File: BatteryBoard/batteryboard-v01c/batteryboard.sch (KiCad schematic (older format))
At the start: 27 parts, among them J1 KEYSTONE-1042, J12 Screw_Terminal_01x02, J2 KEYSTONE-1042, J3 KEYSTONE-1042, J4 KEYSTONE-1042, J5 KEYSTONE-1042, J6 KEYSTONE-1042, J7 5023520400, J8 Screw_Terminal_01x02, Q1 IRF7458, Q2 IRF7458, U1 R5460N233AF

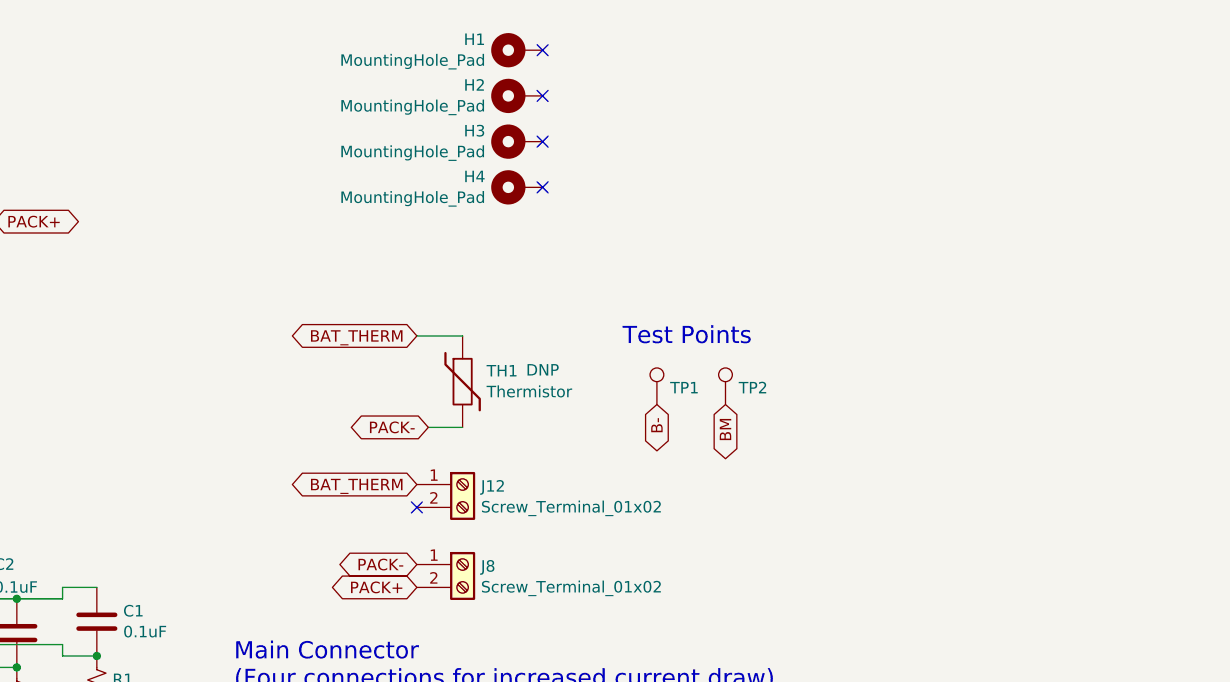
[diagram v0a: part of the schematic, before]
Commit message: Added simple thermistor circuit with logic switch to activate.
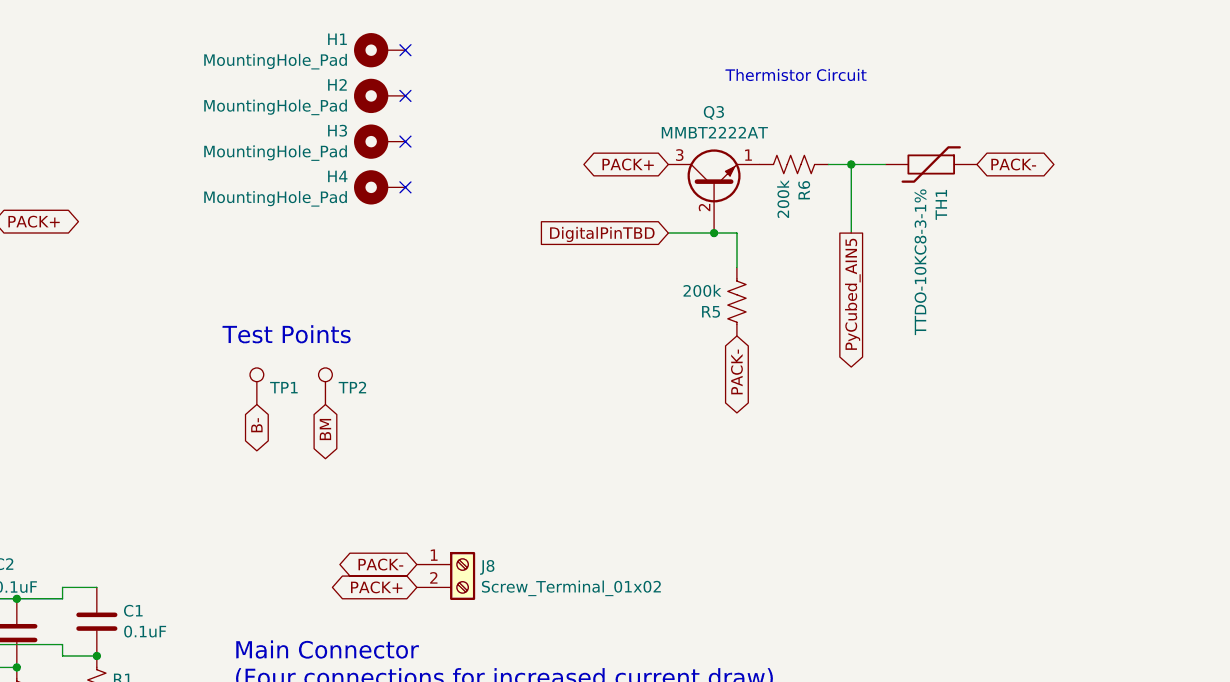
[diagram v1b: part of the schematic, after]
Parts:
- removed J12: Screw_Terminal_01x02, batteryboard:pheonix_2pos_screwterminal, symbol Connector:Screw_Terminal_01x02
- added Q3: MMBT2222AT, Package_TO_SOT_THT:TO-39-3, symbol Transistor_BJT:2N2219
- added R5, R6: 200k, Resistor_SMD:R_0603_1608Metric, symbol Device:R_US
- TH1: value Thermistor -> TTDO-10KC8-3-1%; DNP DNP -> (none)
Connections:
- net BAT_THERM is gone; now on net PACK-: TH1.1
- net PACK+: now also Q3.3 (C)
- net PACK-: now also R5.2; no longer TH1.2
- new net: Q3.1 (E), R6.1
- new net DigitalPinTBD: Q3.2 (B), R5.1
- new net PyCubed_AIN5: R6.2, TH1.2
- no-connect marks 5 -> 4
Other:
- note added: "Thermistor Circuit"
- moved on the sheet: H1, H2, H3, H4, TP1, TP2
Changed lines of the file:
@@
 L Connector:TestPoint TP1
 U 1 1 5E18DFC3
-P 6650 2550
-F 0 "TP1" H 6708 2622 50  0000 L CNN
-F 1 "TestPoint" H 6708 2577 50  0001 L CNN
-F 2 "TestPoint:TestPoint_Loop_D1.80mm_Drill1.0mm_Beaded" H 6850 2550 50  0001 C CNN
-F 3 "~" H 6850 2550 50  0001 C CNN
-F 4 "DNP" H 6650 2550 50  0001 C CNN "DNP"
-	1    6650 2550
+P 4900 2550
+F 0 "TP1" H 4958 2622 50  0000 L CNN
+F 1 "TestPoint" H 4958 2577 50  0001 L CNN
+F 2 "TestPoint:TestPoint_Loop_D1.80mm_Drill1.0mm_Beaded" H 5100 2550 50  0001 C CNN
+F 3 "~" H 5100 2550 50  0001 C CNN
+F 4 "DNP" H 4900 2550 50  0001 C CNN "DNP"
+	1    4900 2550
 	1    0    0    -1
 $EndComp
@@
 L Connector:TestPoint TP2
 U 1 1 5E18E53B
-P 6950 2550
-F 0 "TP2" H 7008 2622 50  0000 L CNN
-F 1 "TestPoint" H 7008 2577 50  0001 L CNN
-F 2 "TestPoint:TestPoint_Loop_D1.80mm_Drill1.0mm_Beaded" H 7150 2550 50  0001 C CNN
-F 3 "~" H 7150 2550 50  0001 C CNN
-F 4 "DNP" H 6950 2550 50  0001 C CNN "DNP"
-	1    6950 2550
-	1    0    0    -1
-$EndComp
-Text GLabel 6650 2550 3    50   BiDi ~ 0
+P 5200 2550
+F 0 "TP2" H 5258 2622 50  0000 L CNN
+F 1 "TestPoint" H 5258 2577 50  0001 L CNN
+F 2 "TestPoint:TestPoint_Loop_D1.80mm_Drill1.0mm_Beaded" H 5400 2550 50  0001 C CNN
+F 3 "~" H 5400 2550 50  0001 C CNN
+F 4 "DNP" H 5200 2550 50  0001 C CNN "DNP"
+	1    5200 2550
+	1    0    0    -1
+$EndComp
+Text GLabel 4900 2550 3    50   BiDi ~ 0
 B-
-Text GLabel 6950 2550 3    50   BiDi ~ 0
+Text GLabel 5200 2550 3    50   BiDi ~ 0
 BM
 Text GLabel 5600 3250 0    50   BiDi ~ 0
@@
 Text GLabel 5600 3350 0    50   BiDi ~ 0
 PACK+
-$Comp
-L Device:Thermistor TH1
-U 1 1 5E1E69F6
-P 5800 2450
-F 0 "TH1" H 5905 2496 50  0000 L CNN
-F 1 "Thermistor" H 5905 2405 50  0000 L CNN
-F 2 "Resistor_THT:R_Axial_DIN0204_L3.6mm_D1.6mm_P5.08mm_Horizontal" H 5800 2450 50  0001 C CNN
-F 3 "~" H 5800 2450 50  0001 C CNN
-F 4 "DNP" H 6150 2500 50  0000 C CNN "DNP"
-	1    5800 2450
-	1    0    0    -1
-$EndComp
-Text GLabel 5650 2650 0    50   BiDi ~ 0
-PACK-
-Wire Wire Line
-	5650 2650 5800 2650
-Text GLabel 5600 2250 0    50   BiDi ~ 0
-BAT_THERM
-Wire Wire Line
-	5600 2250 5800 2250
-Text GLabel 5600 2900 0    50   BiDi ~ 0
-BAT_THERM
 Text Notes 1650 950  0    50   ~ 0
 Must install low-side before high-side
@@
 Text Notes 1650 2550 0    50   ~ 0
 One from this \ngroup first
-Text Notes 6500 2300 0    75   ~ 0
+Text Notes 4750 2300 0    75   ~ 0
 Test Points
 Text Notes 2350 3050 0    75   ~ 0
@@
 L Mechanical:MountingHole_Pad H1
 U 1 1 5E6C3943
-P 6050 1000
-F 0 "H1" V 6004 1150 50  0000 L CNN
-F 1 "MountingHole_Pad" V 6095 1150 50  0000 L CNN
-F 2 "custom-footprints:MountingHole_3.2mm_M3_DIN965_PadMOD" H 6050 1000 50  0001 C CNN
-F 3 "~" H 6050 1000 50  0001 C CNN
-F 4 "DNP" H 6050 1000 50  0001 C CNN "DNP"
-	1    6050 1000
+P 5450 1000
+F 0 "H1" V 5404 1150 50  0000 L CNN
+F 1 "MountingHole_Pad" V 5495 1150 50  0000 L CNN
+F 2 "custom-footprints:MountingHole_3.2mm_M3_DIN965_PadMOD" H 5450 1000 50  0001 C CNN
+F 3 "~" H 5450 1000 50  0001 C CNN
+F 4 "DNP" H 5450 1000 50  0001 C CNN "DNP"
+	1    5450 1000
 	0    -1   1    0
 $EndComp
@@
 L Mechanical:MountingHole_Pad H2
 U 1 1 5E6C65C6
-P 6050 1200
-F 0 "H2" V 6004 1350 50  0000 L CNN
-F 1 "MountingHole_Pad" V 6095 1350 50  0000 L CNN
-F 2 "custom-footprints:MountingHole_3.2mm_M3_DIN965_PadMOD" H 6050 1200 50  0001 C CNN
-F 3 "~" H 6050 1200 50  0001 C CNN
-F 4 "DNP" H 6050 1200 50  0001 C CNN "DNP"
-	1    6050 1200
+P 5450 1200
+F 0 "H2" V 5404 1350 50  0000 L CNN
+F 1 "MountingHole_Pad" V 5495 1350 50  0000 L CNN
+F 2 "custom-footprints:MountingHole_3.2mm_M3_DIN965_PadMOD" H 5450 1200 50  0001 C CNN
+F 3 "~" H 5450 1200 50  0001 C CNN
+F 4 "DNP" H 5450 1200 50  0001 C CNN "DNP"
+	1    5450 1200
 	0    -1   1    0
 $EndComp
@@
 L Mechanical:MountingHole_Pad H3
 U 1 1 5E6C7B02
-P 6050 1400
-F 0 "H3" V 6004 1550 50  0000 L CNN
-F 1 "MountingHole_Pad" V 6095 1550 50  0000 L CNN
-F 2 "custom-footprints:MountingHole_3.2mm_M3_DIN965_PadMOD" H 6050 1400 50  0001 C CNN
-F 3 "~" H 6050 1400 50  0001 C CNN
-F 4 "DNP" H 6050 1400 50  0001 C CNN "DNP"
-	1    6050 1400
+P 5450 1400
+F 0 "H3" V 5404 1550 50  0000 L CNN
+F 1 "MountingHole_Pad" V 5495 1550 50  0000 L CNN
+F 2 "custom-footprints:MountingHole_3.2mm_M3_DIN965_PadMOD" H 5450 1400 50  0001 C CNN
+F 3 "~" H 5450 1400 50  0001 C CNN
+F 4 "DNP" H 5450 1400 50  0001 C CNN "DNP"
+	1    5450 1400
 	0    -1   1    0
 $EndComp
@@
 L Mechanical:MountingHole_Pad H4
 U 1 1 5E6C7E13
-P 6050 1600
-F 0 "H4" V 6004 1750 50  0000 L CNN
-F 1 "MountingHole_Pad" V 6095 1750 50  0000 L CNN
-F 2 "custom-footprints:MountingHole_3.2mm_M3_DIN965_PadMOD" H 6050 1600 50  0001 C CNN
-F 3 "~" H 6050 1600 50  0001 C CNN
-F 4 "DNP" H 6050 1600 50  0001 C CNN "DNP"
-	1    6050 1600
-	0    -1   1    0
-$EndComp
-NoConn ~ 6150 1000
-NoConn ~ 6150 1200
-NoConn ~ 6150 1400
-NoConn ~ 6150 1600
+P 5450 1600
+F 0 "H4" V 5404 1750 50  0000 L CNN
+F 1 "MountingHole_Pad" V 5495 1750 50  0000 L CNN
+F 2 "custom-footprints:MountingHole_3.2mm_M3_DIN965_PadMOD" H 5450 1600 50  0001 C CNN
+F 3 "~" H 5450 1600 50  0001 C CNN
+F 4 "DNP" H 5450 1600 50  0001 C CNN "DNP"
+	1    5450 1600
+	0    -1   1    0
+$EndComp
+NoConn ~ 5550 1000
+NoConn ~ 5550 1200
+NoConn ~ 5550 1400
+NoConn ~ 5550 1600
 Text GLabel 6900 4300 2    50   BiDi ~ 0
 PACK-
@@
 Text GLabel 5300 4300 0    50   BiDi ~ 0
 PACK+
-NoConn ~ 5600 3000
-$Comp
-L Connector:Screw_Terminal_01x02 J12
-U 1 1 5E1A7D63
-P 5800 2900
-F 0 "J12" H 5880 2892 50  0000 L CNN
-F 1 "Screw_Terminal_01x02" H 5880 2801 50  0000 L CNN
-F 2 "batteryboard:pheonix_2pos_screwterminal" H 5800 2900 50  0001 C CNN
-F 3 "~" H 5800 2900 50  0001 C CNN
-F 4 "DNP" H 5800 2900 50  0001 C CNN "DNP"
-	1    5800 2900
-	1    0    0    -1
-$EndComp
 $Comp
 L Connector:Screw_Terminal_01x02 J8
@@
 	1    0    0    -1
 $EndComp
+Text Notes 6950 1150 0    50   ~ 0
+Thermistor Circuit
+Text GLabel 6700 1500 0    50   BiDi ~ 0
+PACK+
+$Comp
+L Transistor_BJT:2N2219 Q3
+U 1 1 6221ACAF
+P 6900 1600
+F 0 "Q3" V 7228 1600 50  0000 C CNN
+F 1 "MMBT2222AT" V 7137 1600 50  0000 C CNN
+F 2 "Package_TO_SOT_THT:TO-39-3" H 7100 1525 50  0001 L CIN
+F 3 "http://www.onsemi.com/pub_link/Collateral/2N2219-D.PDF" H 6900 1600 50  0001 L CNN
+	1    6900 1600
+	0    -1   -1   0
+$EndComp
+$Comp
+L Device:R_US R6
+U 1 1 6221CAB9
+P 7250 1500
+F 0 "R6" H 7182 1454 50  0000 R CNN
+F 1 "200k" H 7182 1545 50  0000 R CNN
+F 2 "Resistor_SMD:R_0603_1608Metric" V 7290 1490 50  0001 C CNN
+F 3 "~" H 7250 1500 50  0001 C CNN
+	1    7250 1500
+	0    -1   -1   0
+$EndComp
+Wire Wire Line
+	7400 1500 7500 1500
+Wire Wire Line
+	7500 1500 7500 1800
+Wire Wire Line
+	7500 1500 7650 1500
+Connection ~ 7500 1500
+Text GLabel 8050 1500 2    50   BiDi ~ 0
+PACK-
+Text GLabel 7500 1800 3    50   Output ~ 0
+PyCubed_AIN5
+Text GLabel 6700 1800 0    50   Input ~ 0
+DigitalPinTBD
+Wire Wire Line
+	6700 1800 6900 1800
+Wire Wire Line
+	6900 1800 7000 1800
+Wire Wire Line
+	7000 1800 7000 1950
+Connection ~ 6900 1800
+$Comp
+L Device:R_US R5
+U 1 1 62221293
+P 7000 2100
+F 0 "R5" H 6932 2054 50  0000 R CNN
+F 1 "200k" H 6932 2145 50  0000 R CNN
+F 2 "Resistor_SMD:R_0603_1608Metric" V 7040 2090 50  0001 C CNN
+F 3 "~" H 7000 2100 50  0001 C CNN
+	1    7000 2100
+	1    0    0    -1
+$EndComp
+Text GLabel 7000 2250 3    50   BiDi ~ 0
+PACK-
+$Comp
+L Device:Thermistor TH1
+U 1 1 62221BFE
+P 7850 1500
+F 0 "TH1" H 7955 1546 50  0000 L CNN
+F 1 "TTDO-10KC8-3-1%" H 7955 1455 50  0000 L CNN
+F 2 "Resistor_THT:R_Axial_DIN0204_L3.6mm_D1.6mm_P5.08mm_Horizontal" H 7850 1500 50  0001 C CNN
+F 3 "~" H 7850 1500 50  0001 C CNN
+F 4 "" H 8200 1550 50  0000 C CNN "DNP"
+	1    7850 1500
+	0    1    1    0
+$EndComp
 $EndSCHEMATC
